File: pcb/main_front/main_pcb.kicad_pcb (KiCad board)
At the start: 2 copper layers, 304.8 x 160.2 mm, 296 parts, among them J1 AVR-ISP-6, J2 USB_C_Receptacle_USB2.0, J3 Conn_01x16_Male, Q1 Q_NMOS_DGS, SW1 RESET, SW2 BOOT, SW3 BL_STEP, U1 ATmega32-16PU, Y1 Crystal

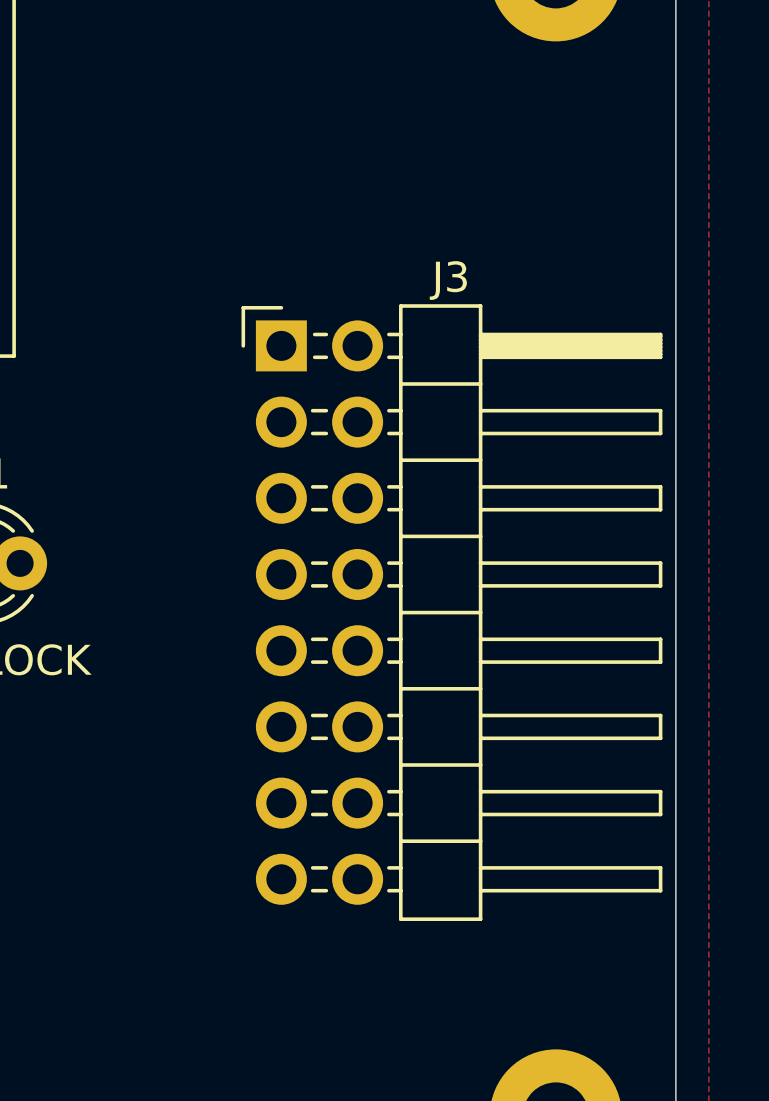
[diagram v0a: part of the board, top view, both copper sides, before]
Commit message: flushed connector, centered
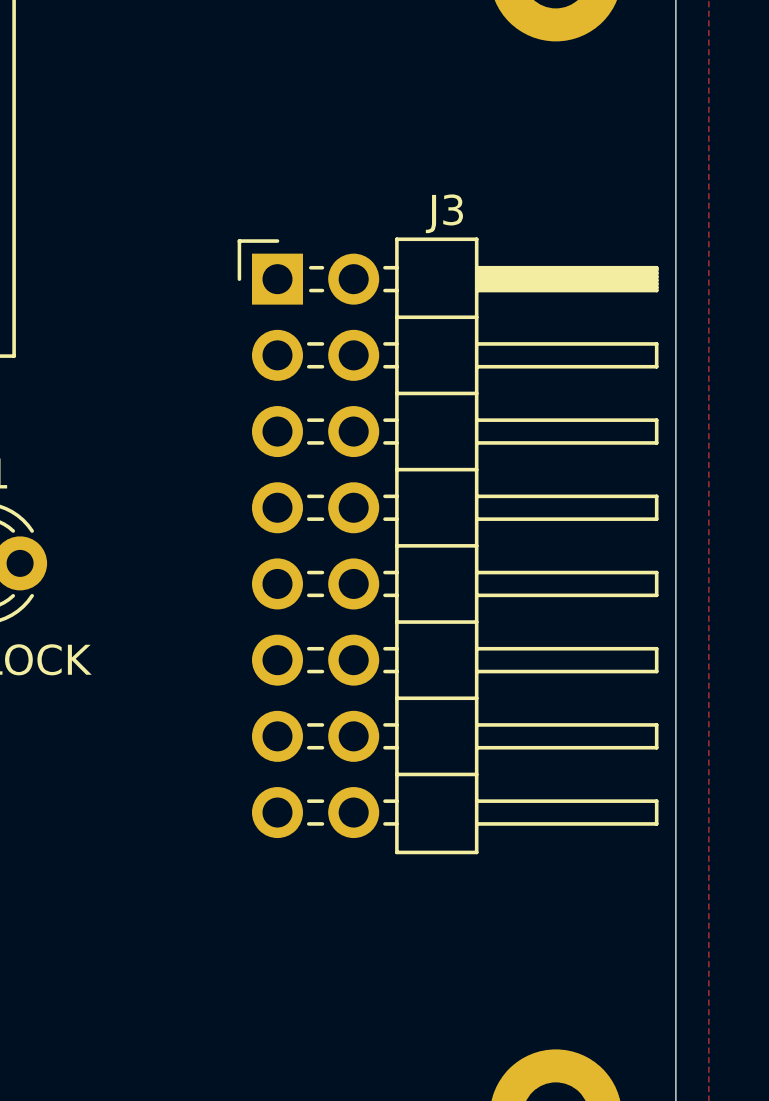
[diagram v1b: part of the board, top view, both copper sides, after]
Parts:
- moved J3 2.23 mm to (434.5, 148.3)
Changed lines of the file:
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@@
   )
   (module Connector_PinHeader_2.54mm:PinHeader_2x08_P2.54mm_Horizontal (layer F.Cu)
-    (at 434.65 150.55)
+    (at 434.52 148.325)
     (descr "Through hole angled pin header, 2x08, 2.54mm pitch, 6mm pin length, double rows")
     (tags "Through hole angled pin header THT 2x08 2.54mm double row")

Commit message: Cleanup
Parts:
- removed the REF** at (300.1, 285.0)
- removed the REF** at (247.0, 138.2)
- removed the REF** at (147.0, 176.2)
- removed the REF** at (443.8, 176.2)
- removed the REF** at (443.8, 138.2)
- removed the REF** at (295.3, 199.2)
- removed the REF** at (162.0, 199.1)
- removed the REF** at (428.7, 199.2)
- removed the REF** at (428.7, 275.3)
- removed the REF** at (166.7, 284.9)
- removed the REF** at (344.8, 176.2)
- removed the REF** at (344.8, 138.2)
- removed the REF** at (247.0, 176.2)
- added REF**: MountingHole_2.2mm_M2_Pad, MountingHole:MountingHole_2.2mm_M2_Pad, F.Cu at (216.6, 210.0)
- added REF**: MountingHole_2.2mm_M2_Pad, MountingHole:MountingHole_2.2mm_M2_Pad, F.Cu at (163.5, 63.2)
- added REF**: MountingHole_2.2mm_M2_Pad, MountingHole:MountingHole_2.2mm_M2_Pad, F.Cu at (63.5, 101.2)
- added REF**: MountingHole_2.2mm_M2_Pad, MountingHole:MountingHole_2.2mm_M2_Pad, F.Cu at (360.3, 101.2)
- added REF**: MountingHole_2.2mm_M2_Pad, MountingHole:MountingHole_2.2mm_M2_Pad, F.Cu at (360.3, 63.2)
- added REF**: MountingHole_2.2mm_M2_Pad, MountingHole:MountingHole_2.2mm_M2_Pad, F.Cu at (211.8, 124.2)
- added REF**: MountingHole_2.2mm_M2_Pad, MountingHole:MountingHole_2.2mm_M2_Pad, F.Cu at (78.5, 124.1)
- added REF**: MountingHole_2.2mm_M2_Pad, MountingHole:MountingHole_2.2mm_M2_Pad, F.Cu at (345.2, 124.2)
- added REF**: MountingHole_2.2mm_M2_Pad, MountingHole:MountingHole_2.2mm_M2_Pad, F.Cu at (345.2, 200.3)
- added REF**: MountingHole_2.2mm_M2_Pad, MountingHole:MountingHole_2.2mm_M2_Pad, F.Cu at (83.2, 209.9)
- added REF**: MountingHole_2.2mm_M2_Pad, MountingHole:MountingHole_2.2mm_M2_Pad, F.Cu at (261.3, 101.2)
- added REF**: MountingHole_2.2mm_M2_Pad, MountingHole:MountingHole_2.2mm_M2_Pad, F.Cu at (261.3, 63.2)
- added REF**: MountingHole_2.2mm_M2_Pad, MountingHole:MountingHole_2.2mm_M2_Pad, F.Cu at (163.5, 101.2)
- moved D3 118.9 mm to (226.2, 61.3)
- moved D4 118.6 mm to (226.2, 64.9)
- moved C1 118.6 mm to (220.9, 63.3)
- moved D1 117.9 mm to (348.4, 66.8)
- moved R2 113.2 mm to (288.9, 89.8)
- moved R1 112.9 mm to (292.4, 89.8)
- moved D5 112.6 mm to (201.2, 63.3)
- moved MX73 112.2 mm to (111.8, 190.8)
- moved MX78 112.2 mm to (207.1, 190.8)
- moved C4 112.2 mm to (335.9, 84.3)
- moved C5 112.2 mm to (319.9, 84.3)
- moved D10 112.2 mm to (114.9, 91.8)
- moved D105 112.2 mm to (272.4, 91.8)
- moved D11 112.2 mm to (127.4, 89.8)
- moved D12 112.2 mm to (139.9, 87.8)
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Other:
- board text added: "BACKLIGHT"
- board text added: "GND"
- board text added: "MISO"
- board text added: "MOSI"
- board text added: "NUMPAD CONNECTOR"
- board text added: "RST"
- board text added: "SCK"
- board text added: "VCC"

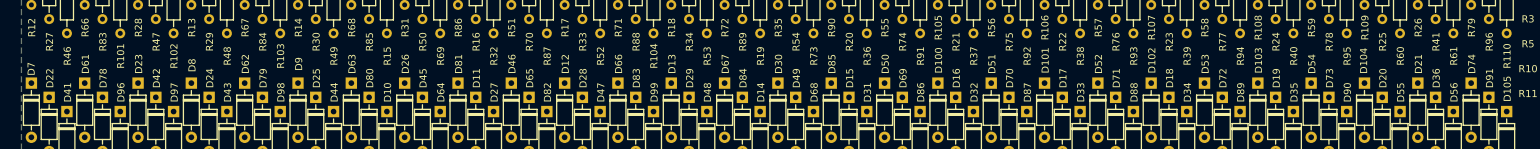
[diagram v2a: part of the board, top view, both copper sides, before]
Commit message: reordered diodes to allow for easier traces
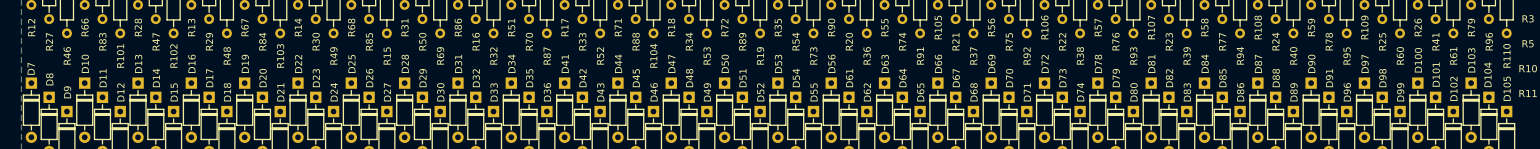
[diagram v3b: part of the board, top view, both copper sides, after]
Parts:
- moved D96 172.5 mm to (249.9, 91.8)
- moved D97 167.5 mm to (252.4, 87.8)
- moved D21 160.0 mm to (99.9, 91.8)
- moved D20 157.5 mm to (97.4, 89.8)
- moved D98 155.0 mm to (254.9, 89.8)
- moved D19 145.0 mm to (94.9, 87.8)
- moved D78 140.0 mm to (214.9, 87.8)
- moved D18 132.5 mm to (92.4, 91.8)
- moved D36 125.0 mm to (137.4, 91.8)
- moved D17 120.0 mm to (89.9, 89.8)
- moved D79 120.0 mm to (217.4, 89.8)
- moved D16 107.5 mm to (87.4, 87.8)
- moved D35 107.5 mm to (134.9, 89.8)
- moved D61 107.5 mm to (179.9, 89.8)
- moved D80 107.5 mm to (219.9, 91.8)
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
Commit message: began traces on main board
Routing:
- net LEDGND: track 0.00 -> 2064.1 mm
- net +5V: track 0.00 -> 391.2 mm
- net col13: track 0.00 -> 133.2 mm
- net col12: track 0.00 -> 115.4 mm
- net col10: track 0.00 -> 114.0 mm
- net col11: track 0.00 -> 113.9 mm
- net col9: track 0.00 -> 112.3 mm
- net col2: track 0.00 -> 108.1 mm
- net col6: track 0.00 -> 106.1 mm
- net col0: track 0.00 -> 104.1 mm
- net col1: track 0.00 -> 98.3 mm
- net col15: track 0.00 -> 95.3 mm
- net col8: track 0.00 -> 86.1 mm
- net col5: track 0.00 -> 86.1 mm
- net col3: track 0.00 -> 86.1 mm
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- added copper zone on B.Cu, net GND
- removed copper zone on B.Cu, net +5V
- removed copper zone on B.Cu, net LEDGND

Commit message: Rearrange main board diodes
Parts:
- removed the REF** at (163.5, 63.2)
- removed the REF** at (261.3, 101.2)
- removed the REF** at (261.3, 63.2)
- removed the REF** at (163.5, 101.2)
- added REF**: MountingHole_2.2mm_M2_Pad, MountingHole:MountingHole_2.2mm_M2_Pad, F.Cu at (160.5, 101.2)
- added REF**: MountingHole_2.2mm_M2_Pad, MountingHole:MountingHole_2.2mm_M2_Pad, F.Cu at (160.5, 63.2)
- added REF**: MountingHole_2.2mm_M2_Pad, MountingHole:MountingHole_2.2mm_M2_Pad, F.Cu at (264.3, 101.2)
- added REF**: MountingHole_2.2mm_M2_Pad, MountingHole:MountingHole_2.2mm_M2_Pad, F.Cu at (264.3, 63.2)
- moved D96 172.5 mm to (77.4, 93.8)
- moved D97 167.5 mm to (84.9, 87.8)
- moved D21 160.2 mm to (259.9, 83.8)
- moved D20 157.6 mm to (254.9, 83.8)
- moved D98 155.1 mm to (99.9, 93.8)
- moved D19 145.1 mm to (239.9, 83.8)
- moved D78 140.1 mm to (74.9, 91.8)
- moved D18 132.7 mm to (224.9, 83.8)
- moved D36 125.1 mm to (262.4, 85.8)
- moved D17 120.1 mm to (209.9, 83.8)
- moved D79 120.0 mm to (97.4, 91.8)
- moved D16 107.6 mm to (194.9, 83.8)
- moved D35 107.6 mm to (242.4, 85.8)
- moved D61 107.5 mm to (72.4, 89.8)
- moved D80 107.5 mm to (112.4, 91.8)
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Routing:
- net LEDGND: track 2064.1 -> 40.1 mm
- net Net-(D4-Pad1): track 77.4 -> 0.11 mm
- net Net-(D3-Pad1): track 17.8 -> 0.11 mm
- net NUMLOCK: track 57.6 -> 51.9 mm
